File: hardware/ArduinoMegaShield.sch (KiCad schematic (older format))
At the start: 59 parts, among them P1 CONN_01X02, P10 CONN_01X02, P11 CONN_01X02, P12 CONN_01X02, P13 CONN_01X02, P14 CONN_01X02, P15 CONN_01X02, P16 CONN_01X02, P17 CONN_01X02, P18 CONN_01X02, P19 CONN_01X02, P2 CONN_01X02, P20 CONN_01X02, P21 CONN_01X02, P22 CONN_01X02, P23 CONN_01X02, P24 CONN_01X02, P3 CONN_01X02, P4 CONN_01X02, P5 CONN_01X02, P6 CONN_01X02, P7 CONN_01X02, P8 CONN_01X02, P9 CONN_01X02, U1 A4988, U2 A4988, U3 A4988

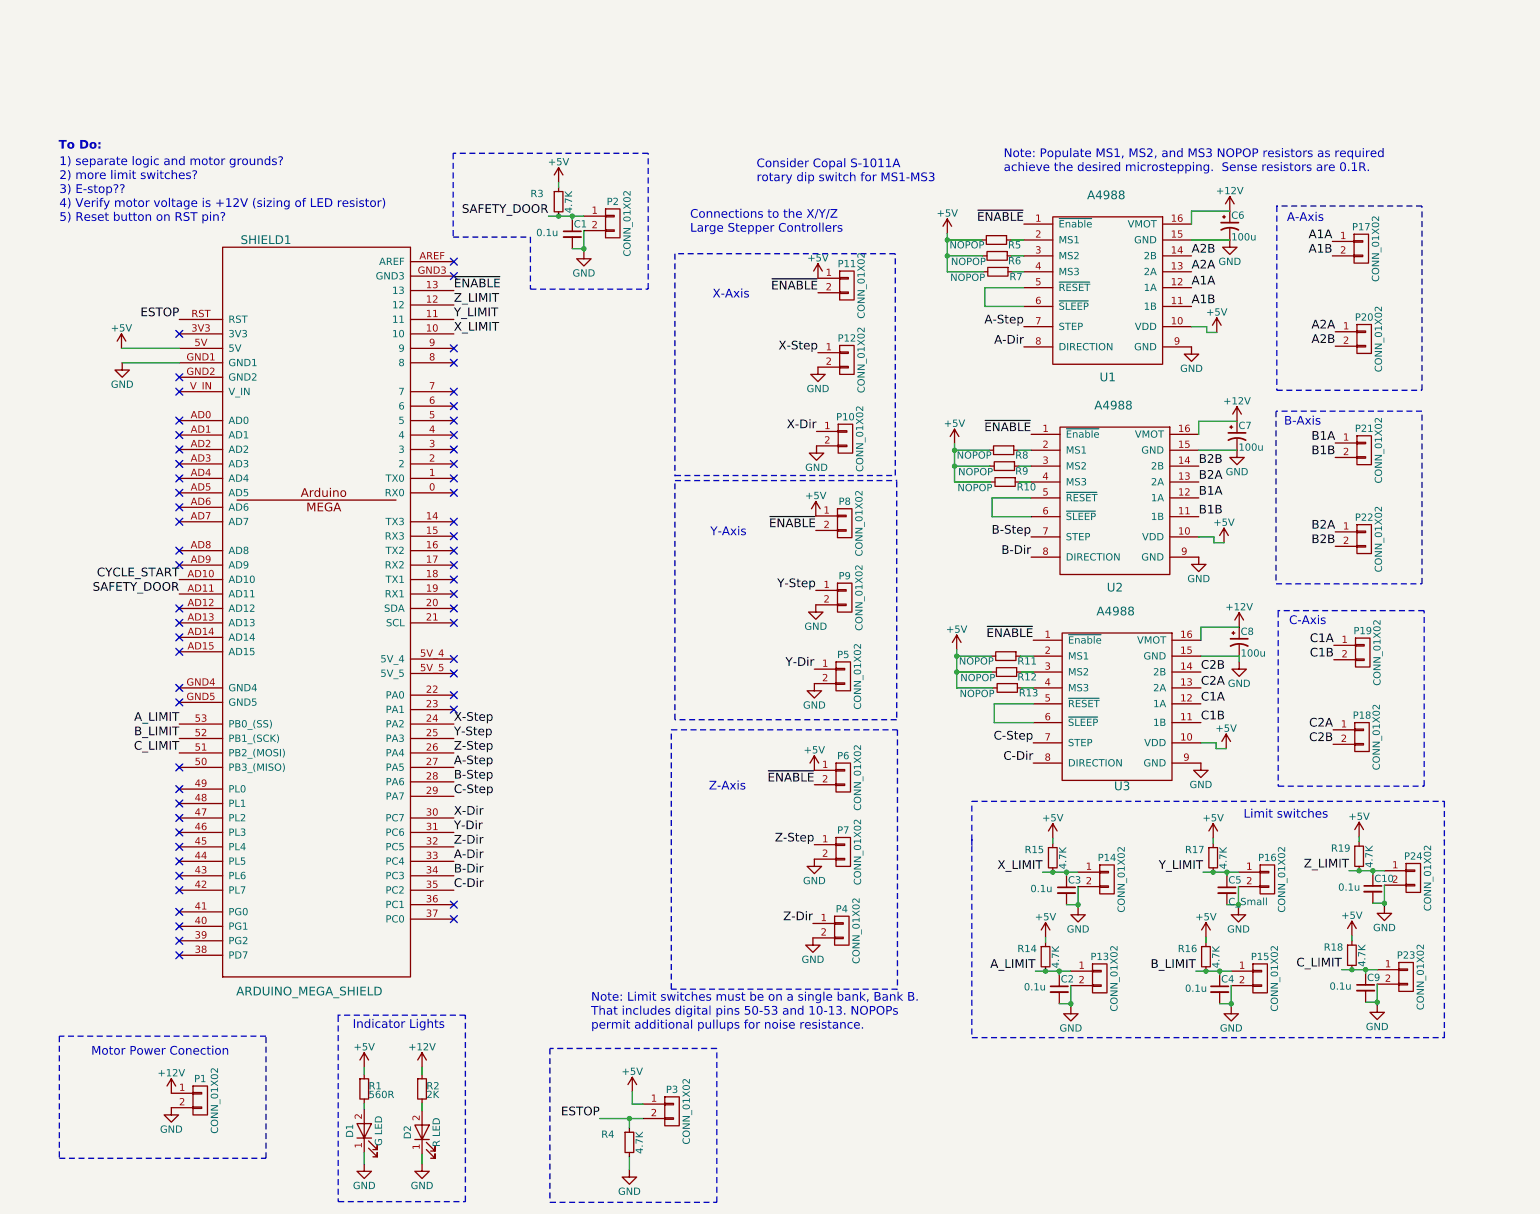
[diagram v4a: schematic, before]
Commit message: added switches for cycle_start and feed_hold, added docs for protoboard mockup
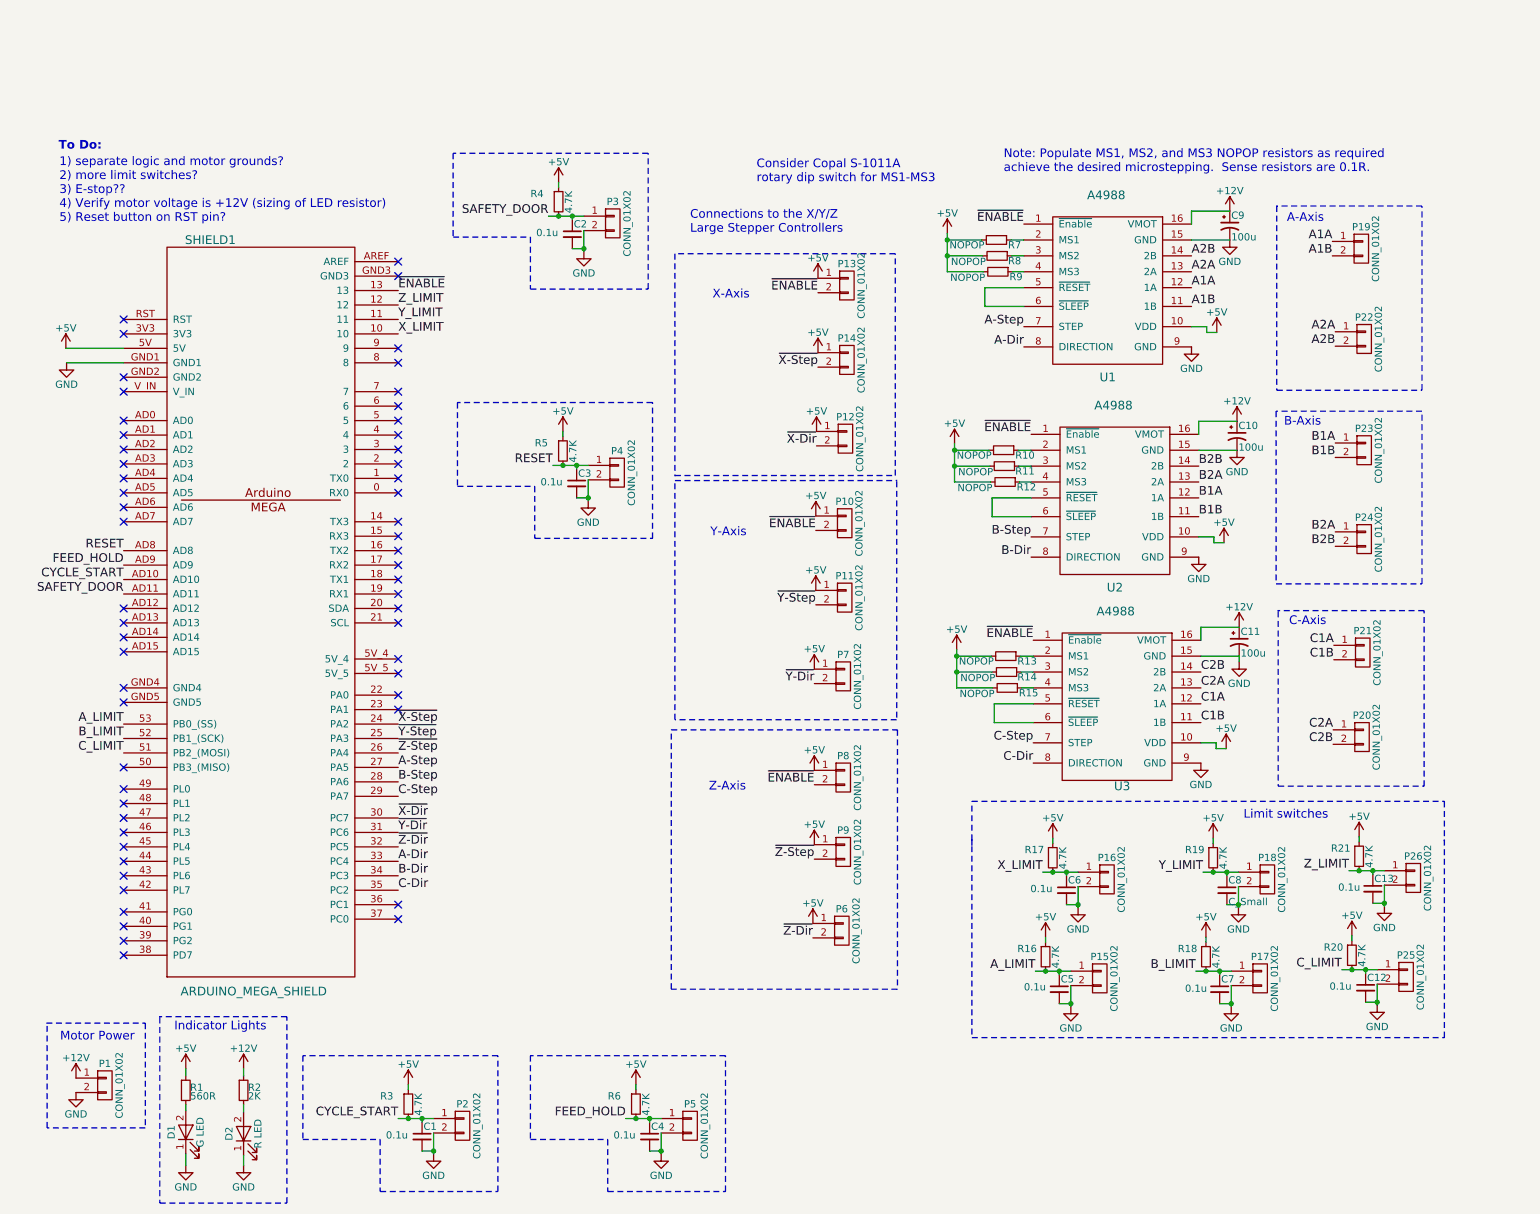
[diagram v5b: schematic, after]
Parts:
- removed P3: CONN_01X02, 6axis:Terminal_Block_200_mil, symbol CONN_01X02
- removed R4: 4.7K, Resistors_SMD:R_0805_HandSoldering, symbol R_Small
- added C1, C3, C4: 0.1u, symbol C_Small
- added P2, P4, P5: CONN_01X02, 6axis:Terminal_Block_200_mil, symbol CONN_01X02
- added R3, R5, R6: 4.7K, Resistors_SMD:R_0805_HandSoldering, symbol R_Small
- renumbered C7 to C10, C8 to C11, C9 to C12, C10 to C13, C1 to C2, C2 to C5, C3 to C6, C4 to C7, C5 to C8, C6 to C9, P8 to P10, P9 to P11, P10 to P12, P11 to P13, P12 to P14, P13 to P15, P14 to P16, P15 to P17, P16 to P18, P17 to P19, P18 to P20, P19 to P21, P20 to P22, P21 to P23, P22 to P24, P23 to P25, P24 to P26, P2 to P3, P4 to P6, P5 to P7, P6 to P8, P7 to P9, R8 to R10, R9 to R11, R10 to R12, R11 to R13, R12 to R14, R13 to R15, R14 to R16, R15 to R17, R16 to R18, R17 to R19, R18 to R20, R19 to R21, R3 to R4, R5 to R7, R6 to R8, R7 to R9
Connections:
- net +5V: now also P11.1 (P1), P12.1 (P1), P14.1 (P1), P6.1 (P1), P7.1 (P1), P9.1 (P1), R3.1, R5.1, R6.1
- net CYCLE_START: now also C1.1, P2.1 (P1), R3.2
- net GND: now also C1.2, C3.2, C4.2, P2.2 (P2), P4.2 (P2), P5.2 (P2); no longer P11.2 (P2), P12.2 (P2), P14.2 (P2), P6.2 (P2), P7.2 (P2), P9.2 (P2)
- net RESET: now reaches SHIELD1.AD8
- net RESET: now also C3.1, P4.1 (P1), R5.2
- net FEED_HOLD: now reaches SHIELD1.AD9
- net FEED_HOLD: now also C4.1, P5.1 (P1), R6.2
- net ESTOP: no longer names the net of SHIELD1.RST
- net X-Dir renamed ~X-Dir
- net ~X-Dir: now also P12.2 (P2); no longer P12.1 (P1)
- net X-Step renamed ~X-Step
- net ~X-Step: now also P14.2 (P2); no longer P14.1 (P1)
- net Y-Dir renamed ~Y-Dir
- net ~Y-Dir: now also P7.2 (P2); no longer P7.1 (P1)
- net Y-Step renamed ~Y-Step
- net ~Y-Step: now also P11.2 (P2); no longer P11.1 (P1)
- net Z-Dir renamed ~Z-Dir
- net ~Z-Dir: now also P6.2 (P2); no longer P6.1 (P1)
- net Z-Step renamed ~Z-Step
- net ~Z-Step: now also P9.2 (P2); no longer P9.1 (P1)
- no-connect marks 58 -> 57
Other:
- note added: "Motor Power"
- note removed: "Motor Power Conection"
- note removed: "Note: Limit switches must be on a single bank, Bank B.\nThat includes digital pins 50-53 and 10-13. NOPOPs\npermit additional pullups for noise resistance."
- moved on the sheet: D1, D2, P1, R1, R2

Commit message: moved connectors to separate sheet and started board layout
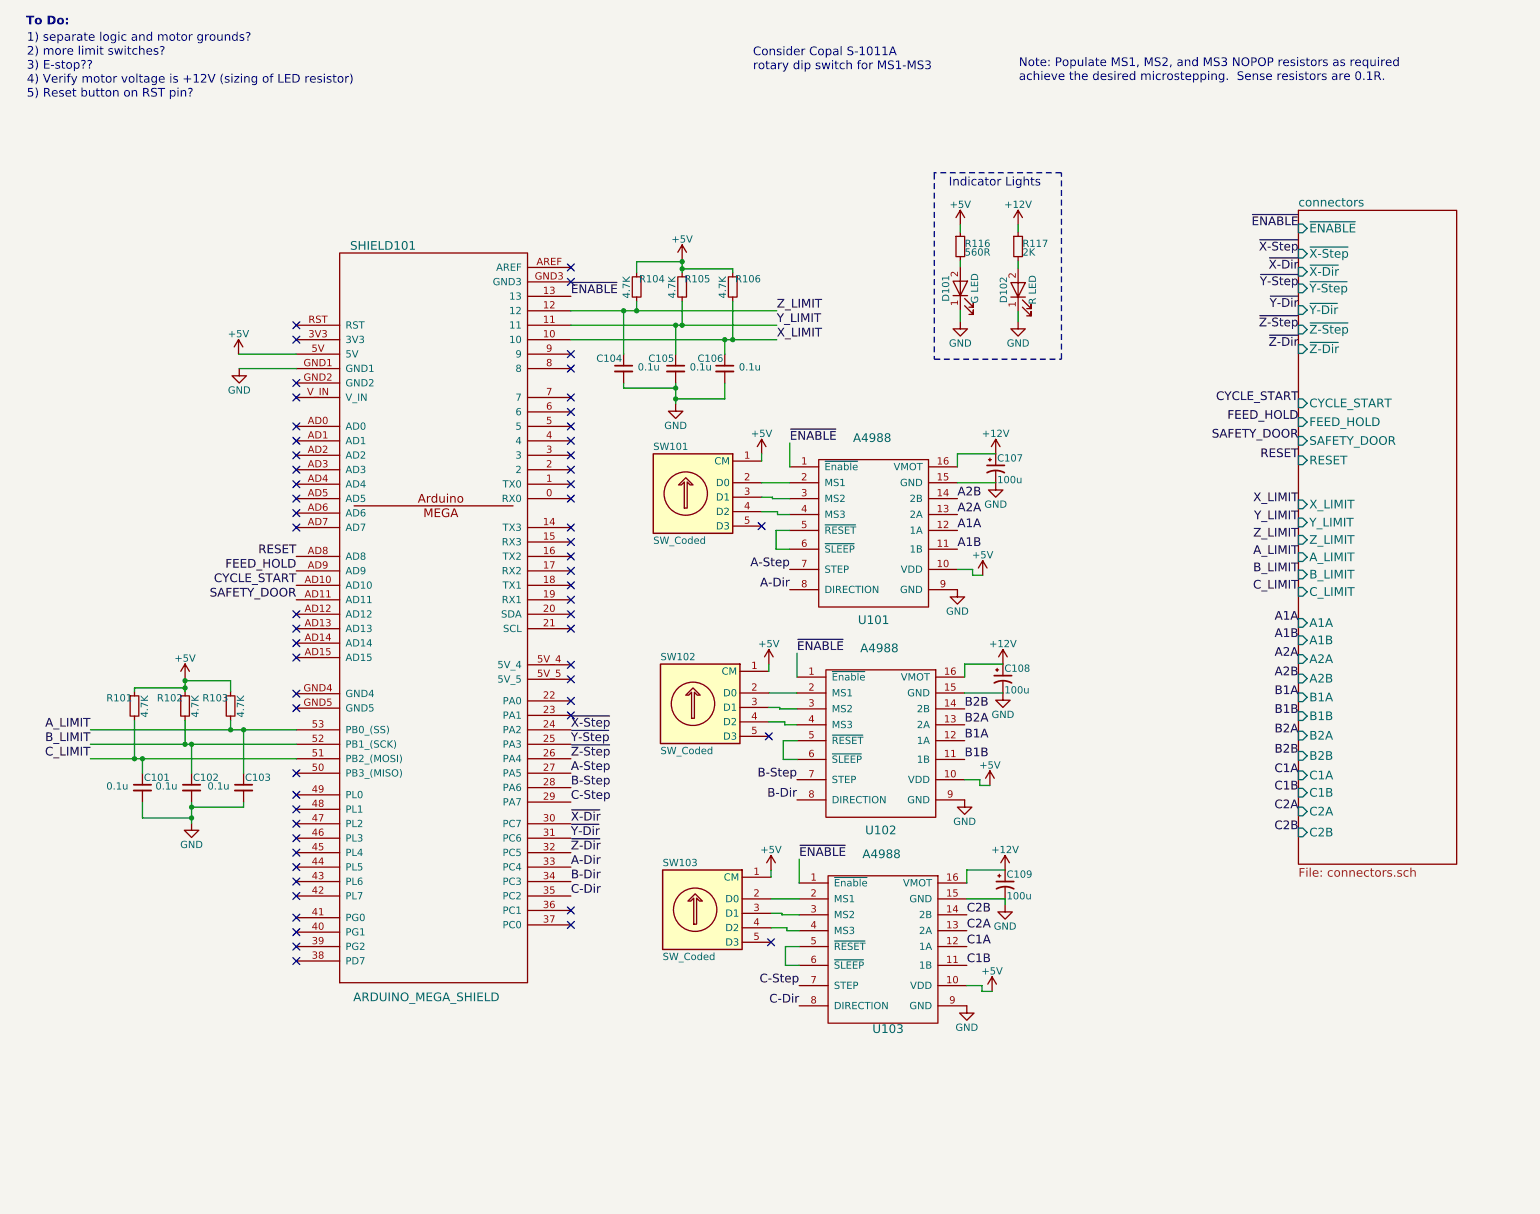
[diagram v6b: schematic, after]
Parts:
- removed C1, C12, C13, C2, C3, C4, C5, C6, C7: 0.1u, symbol C_Small
- removed C8: C_Small, symbol C_Small
- removed D1: G LED, LEDs:LED_0805, symbol LED
- removed D2: R LED, LEDs:LED_0805, symbol LED
- removed P1, P10, P11, P12, P13, P14, P15, P16, P17, P18, P19, P2, P20, P21, P22, P23, P24, P25, P26, P3, P4, P5, P6, P7, P8, P9: CONN_01X02, 6axis:Terminal_Block_200_mil, symbol CONN_01X02
- removed R1: 560R, Resistors_SMD:R_0805_HandSoldering, symbol R_Small
- removed R10, R11, R12, R13, R14, R15, R7, R8, R9: NOPOP, Resistors_SMD:R_0805_HandSoldering, symbol R_Small
- removed R16, R17, R18, R19, R20, R21, R3, R4, R5, R6: 4.7K, Resistors_SMD:R_0805_HandSoldering, symbol R_Small
- removed R2: 2K, Resistors_SMD:R_0805_HandSoldering, symbol R_Small
- added C101, C102, C103, C104, C105, C106: 0.1u, Capacitors_SMD:C_0805_HandSoldering, symbol C_Small
- added D101: G LED, LEDs:LED_0805, symbol LED
- added D102: R LED, LEDs:LED_0805, symbol LED
- added R101, R102, R103, R104, R105, R106: 4.7K, Resistors_SMD:R_0805_HandSoldering, symbol R_Small
- added R116: 560R, Resistors_SMD:R_0805_HandSoldering, symbol R_Small
- added R117: 2K, Resistors_SMD:R_0805_HandSoldering, symbol R_Small
- added SW101, SW102, SW103: SW_Coded, symbol SW_Coded
- renumbered C9 to C107, C10 to C108, C11 to C109, SHIELD1 to SHIELD101, U1 to U101, U2 to U102, U3 to U103
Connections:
- net +12V: now also R117.1
- net +5V: now also R101.1, R102.1, R103.1, R104.1, R105.1, R106.1, R116.1, SW101.1 (CM), SW102.1 (CM), SW103.1 (CM)
- net A_LIMIT: now also C103.1, R103.2
- net B_LIMIT: now also C102.1, R102.2
- net C_LIMIT: now also C101.1, R101.2
- net GND: now also C101.2, C102.2, C103.2, C104.2, C105.2, C106.2, D101.1 (K), D102.1 (K)
- net X_LIMIT: now also C106.1, R106.2
- net Y_LIMIT: now also C105.1, R105.2
- net Z_LIMIT: now also C104.1, R104.2
- net at U101.2 (MS1): now also SW101.2 (D0)
- net at U101.3 (MS2): now also SW101.3 (D1)
- net at U101.4 (MS3): now also SW101.4 (D2)
- net at U102.2 (MS1): now also SW102.2 (D0)
- net at U102.3 (MS2): now also SW102.3 (D1)
- net at U102.4 (MS3): now also SW102.4 (D2)
- net at U103.2 (MS1): now also SW103.2 (D0)
- net at U103.3 (MS2): now also SW103.3 (D1)
- net at U103.4 (MS3): now also SW103.4 (D2)
- new net: D101.2 (A), R116.2
- new net: D102.2 (A), R117.2
- no-connect marks 57 -> 60
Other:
- note removed: "A-Axis"
- note removed: "B-Axis"
- note removed: "C-Axis"
- note removed: "Connections to the X/Y/Z\nLarge Stepper Controllers"
- note removed: "Limit switches"
- note removed: "Motor Power"
- note removed: "X-Axis"
- note removed: "Y-Axis"
- note removed: "Z-Axis"
- moved on the sheet: C107, C108, C109, SHIELD101, U101, U102, U103

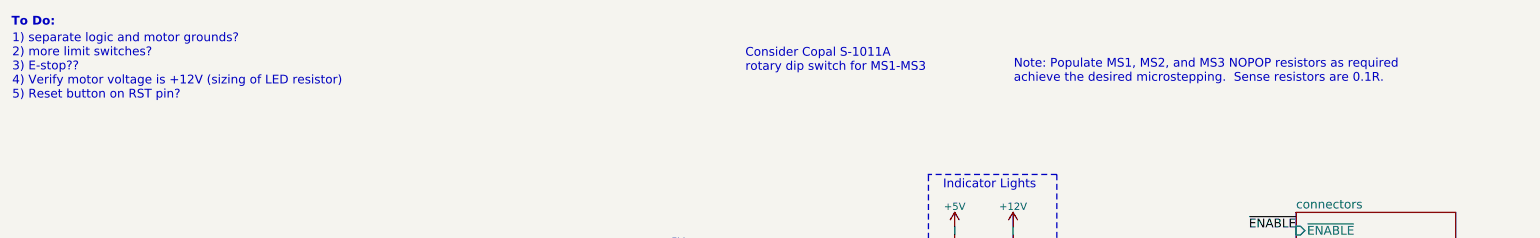
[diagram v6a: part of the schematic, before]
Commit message: updated schematic pdf
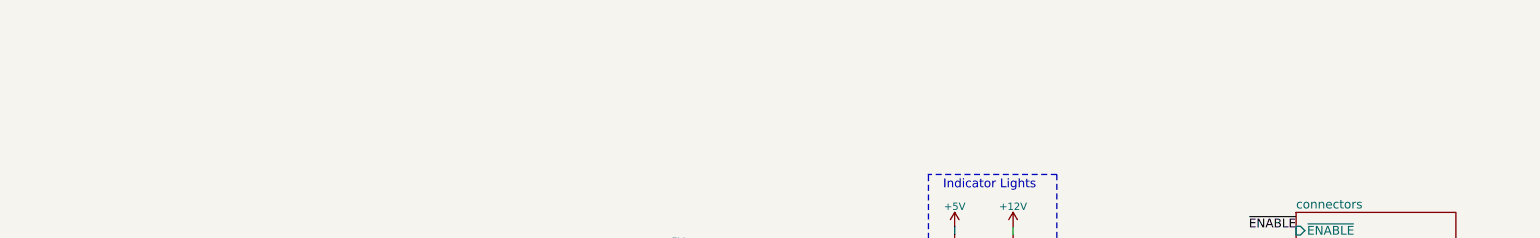
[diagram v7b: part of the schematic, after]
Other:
- note removed: "1) separate logic and motor grounds?\n2) more limit switches?\n3) E-stop??\n4) Verify motor voltage is +12V (sizing of LED resistor)\n5) Reset button on RST pin?"
- note removed: "Consider Copal S-1011A\nrotary dip switch for MS1-MS3"
- note removed: "Note: Populate MS1, MS2, and MS3 NOPOP resistors as required\nachieve the desired microstepping. Sense resistors are 0.1R."
- note removed: "To Do:"
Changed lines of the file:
@@
 Text Label 5840 6340 2    60   ~ 0
 C-Step
-Text Notes 490  -295 0    60   ~ 12
-To Do:
-Text Notes 495  205  0    60   ~ 0
-1) separate logic and motor grounds?\n2) more limit switches?\n3) E-stop??\n4) Verify motor voltage is +12V (sizing of LED resistor)\n5) Reset button on RST pin?
-Text Notes 7360 90   0    60   ~ 0
-Note: Populate MS1, MS2, and MS3 NOPOP resistors as required\nachieve the desired microstepping.  Sense resistors are 0.1R.
 $Comp
 L +5V #PWR013
@@
 	1    0    0    -1
 $EndComp
-Text Notes 5520 15   0    60   ~ 0
-Consider Copal S-1011A\nrotary dip switch for MS1-MS3
 $Comp
 L ARDUINO_MEGA_SHIELD SHIELD101
